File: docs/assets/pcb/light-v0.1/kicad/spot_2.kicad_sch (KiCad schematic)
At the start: 7 parts, among them J10 SPOT 2, J11 SPOT 3, J9 SPOT 1, U500 27V flat-clamp transient prot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

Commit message: Refresh PCB chapters from verified central LED snapshots
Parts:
- C523, C524: Manufacturer (none) -> Murata
- D504: Manufacturer (none) -> Diodes Incorporated
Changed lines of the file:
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@@
         (font
           (size 1.0 1.0))))
-    (property "Manufacturer" ""
+    (property "Manufacturer" "Diodes Incorporated"
       (at 175.26 180.34 0.0)
       (hide yes)
@@
         (font
           (size 1.0 1.0))))
-    (property "Manufacturer" ""
+    (property "Manufacturer" "Murata"
       (at 43.18 180.34 0.0)
       (hide yes)
@@
         (font
           (size 1.0 1.0))))
-    (property "Manufacturer" ""
+    (property "Manufacturer" "Murata"
       (at 96.52 180.34 0.0)
       (hide yes)

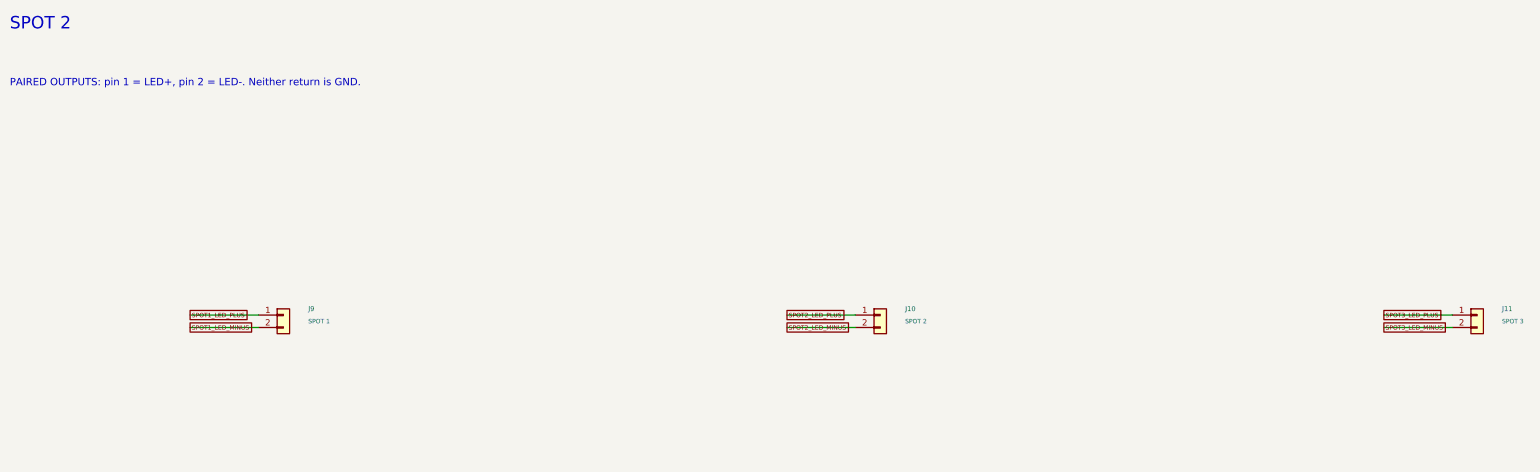
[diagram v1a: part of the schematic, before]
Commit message: Refresh PCB chapters for grouped arm connectors and branded revision
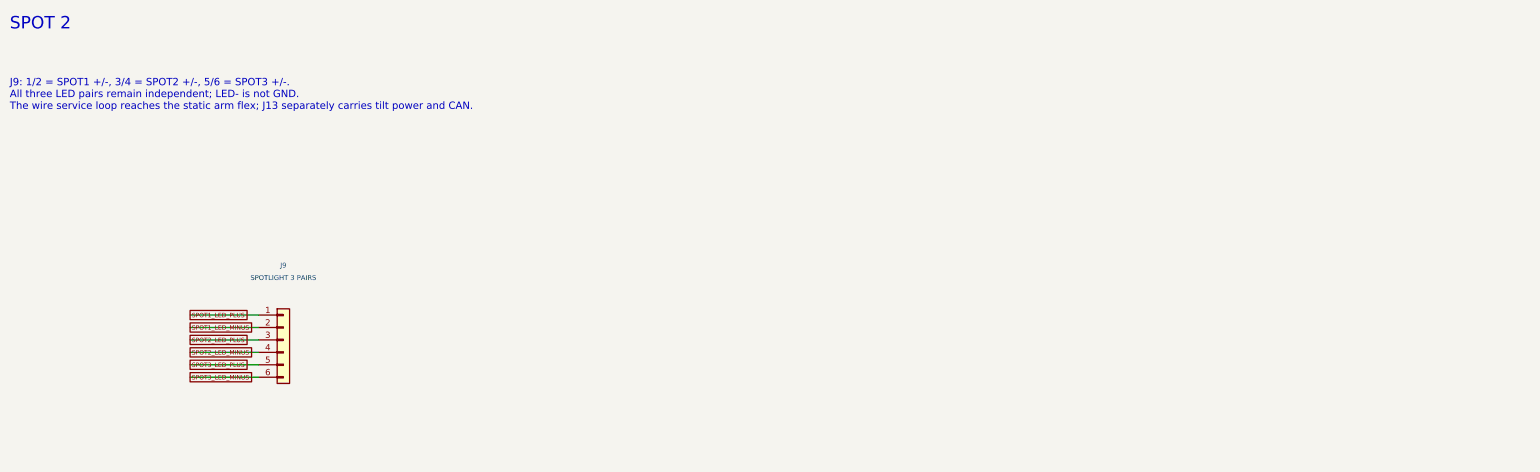
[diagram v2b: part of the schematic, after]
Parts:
- removed J10: SPOT 2, ELF:Enclosure_J10, symbol Connector_Generic:Conn_01x02
- removed J11: SPOT 3, Connector_JST:JST_GH_BM02B-GHS-TBT_1x02-1MP_P1.25mm_Vertical, symbol Connector_Generic:Conn_01x02
- J9: value SPOT 1 -> SPOTLIGHT 3 PAIRS; footprint ELF:Enclosure_J9 -> EL:JST_GH_BM06B-GHS-TBT_1x06-1MP_P1.25mm_Vertical; symbol Connector_Generic:Conn_01x02 -> Connector_Generic:Conn_01x06; MPN BM02B-GHS-TBT(LF)(SN) -> BM06B-GHS-TBT(LF)(SN)
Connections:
- net SPOT2_LED_MINUS: now also J9.4 (Pin_4)
- net SPOT2_LED_PLUS: now also J9.3 (Pin_3)
- net SPOT3_LED_MINUS: now also J9.6 (Pin_6)
- net SPOT3_LED_PLUS: now also J9.5 (Pin_5)
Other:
- note added: "J9: 1/2 = SPOT1 +/-, 3/4 = SPOT2 +/-, 5/6 = SPOT3 +/-. All three LED pairs remain independent; LED- is not GND. The wire service loop reaches the static arm flex; J13 separately carries tilt power and CAN."
- note removed: "PAIRED OUTPUTS: pin 1 = LED+, pin 2 = LED-. Neither return is GND."
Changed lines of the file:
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@@
         (font
           (size 1.0 1.0)))))
+  (wire
+    (pts
+      (xy 43.18 176.53)
+      (xy 96.52 176.53))
+    (stroke
+      (width 0)
+      (type default))
+)
+  (global_label "V24_SPOT"
+    (shape passive)
+    (at 96.52 176.53 0)
+    (effects
+      (font
+        (size 0.9 0.9))
+      (justify left))
+    (property "Intersheetrefs" "${INTERSHEET_REFS}"
+      (at 96.52 176.53 0.0)
+      (hide yes)
+      (effects
+        (font
+          (size 1.0 1.0)))))
+  (text "SPOT 2"
+    (at 20.32 15.24 0)
+    (effects
+      (font
+        (size 2.54 2.54))
+      (justify left top))
+)
+  (text "J9: 1/2 = SPOT1 +/-, 3/4 = SPOT2 +/-, 5/6 = SPOT3 +/-.\nAll three LED pairs remain independent; LED- is not GND.\nThe wire service loop reaches the static arm flex; J13 separately carries tilt power and CAN."
+    (at 20.32 27.94 0)
+    (effects
+      (font
+        (size 1.5 1.5))
+      (justify left top))
+)
+  (text "CH3 current loop continuation from U9 on spot_1"
+    (at 20.32 132.08 0)
+    (effects
+      (font
+        (size 1.8 1.8))
+      (justify left top))
+)
+  (text "U500 local spotlight-rail shunt clamp.\nPulse limits do not establish continuous braking."
+    (at 241.3 228.6 0)
+    (effects
+      (font
+        (size 1.27 1.27))
+      (justify left top))
+)
+  (embedded_fonts no)
   (symbol
-    (lib_id "Connector_Generic:Conn_01x02")
-    (at 76.2 76.2 0)
+    (lib_id "Connector_Generic:Conn_01x06")
+    (at 76.2 81.28 0)
     (unit 1)
     (exclude_from_sim yes)
@@
     (dnp no)
     (property "Reference" "J9"
-      (at 81.28 74.93 0.0)
-      (effects
-        (font
-          (size 1.0 1.0))
-        (justify left)))
-    (property "Value" "SPOT 1"
-      (at 81.28 77.47 0.0)
-      (effects
-        (font
-          (size 0.9 0.9))
-        (justify left)))
-    (property "Footprint" "ELF:Enclosure_J9"
-      (at 76.2 76.2 0.0)
-      (hide yes)
-      (effects
-        (font
-          (size 1.0 1.0))))
-    (property "MPN" "BM02B-GHS-TBT(LF)(SN)"
-      (at 76.2 76.2 0.0)
+      (at 76.2 66.04 0.0)
+      (effects
+        (font
+          (size 1.0 1.0))))
+    (property "Value" "SPOTLIGHT 3 PAIRS"
+      (at 76.2 68.58 0.0)
+      (effects
+        (font
+          (size 1.0 1.0))))
+    (property "Footprint" "EL:JST_GH_BM06B-GHS-TBT_1x06-1MP_P1.25mm_Vertical"
+      (at 76.2 81.28 0.0)
+      (hide yes)
+      (effects
+        (font
+          (size 1.0 1.0))))
+    (property "MPN" "BM06B-GHS-TBT(LF)(SN)"
+      (at 76.2 81.28 0.0)
       (hide yes)
       (effects
@@
           (size 1.0 1.0))))
     (property "Manufacturer" "JST"
-      (at 76.2 76.2 0.0)
+      (at 76.2 81.28 0.0)
       (hide yes)
       (effects
@@
           (size 1.0 1.0))))
     (property "Datasheet" "https://www.jst-mfg.com/product/pdf/eng/eGH.pdf"
-      (at 76.2 76.2 0.0)
+      (at 76.2 81.28 0.0)
       (hide yes)
       (effects
@@
 )
     (pin "2"
+)
+    (pin "3"
+)
+    (pin "4"
+)
+    (pin "5"
+)
+    (pin "6"
 ))
   (wire
@@
         (font
           (size 1.0 1.0)))))
-  (symbol
-    (lib_id "Connector_Generic:Conn_01x02")
-    (at 198.12 76.2 0)
-    (unit 1)
-    (exclude_from_sim yes)
-    (in_bom yes)
-    (on_board yes)
-    (dnp no)
-    (property "Reference" "J10"
-      (at 203.2 74.93 0.0)
-      (effects
-        (font
-          (size 1.0 1.0))
-        (justify left)))
-    (property "Value" "SPOT 2"
-      (at 203.2 77.47 0.0)
-      (effects
-        (font
-          (size 0.9 0.9))
-        (justify left)))
-    (property "Footprint" "ELF:Enclosure_J10"
-      (at 198.12 76.2 0.0)
-      (hide yes)
-      (effects
-        (font
-          (size 1.0 1.0))))
-    (property "MPN" "BM02B-GHS-TBT(LF)(SN)"
-      (at 198.12 76.2 0.0)
-      (hide yes)
-      (effects
-        (font
-          (size 1.0 1.0))))
-    (property "Manufacturer" "JST"
-      (at 198.12 76.2 0.0)
-      (hide yes)
-      (effects
-        (font
-          (size 1.0 1.0))))
-    (property "Datasheet" "https://www.jst-mfg.com/product/pdf/eng/eGH.pdf"
-      (at 198.12 76.2 0.0)
-      (hide yes)
-      (effects
-        (font
-          (size 1.0 1.0))))
-    (instances
-      (project "engineered-lighting-rev-a"
-        (path "/964013ac-cca6-5de7-b648-d598a25a58e0/7d811806-cdea-579b-88fd-298c7067c42f"
-          (reference "J10")
-          (unit 1))))
-    (pin "1"
-)
-    (pin "2"
-))
-  (wire
-    (pts
-      (xy 193.04 76.2)
-      (xy 179.07 76.2))
+  (wire
+    (pts
+      (xy 71.12 81.28)
+      (xy 57.15 81.28))
     (stroke
       (width 0)
@@
   (global_label "SPOT2_LED_PLUS"
     (shape passive)
-    (at 179.07 76.2 0.0)
-    (effects
-      (font
-        (size 0.9 0.9))
-      (justify left))
-    (property "Intersheetrefs" "${INTERSHEET_REFS}"
-      (at 179.07 76.2 0.0)
-      (hide yes)
-      (effects
-        (font
-          (size 1.0 1.0)))))
-  (wire
-    (pts
-      (xy 193.04 78.74)
-      (xy 179.07 78.74))
+    (at 57.15 81.28 0.0)
+    (effects
+      (font
+        (size 0.9 0.9))
+      (justify left))
+    (property "Intersheetrefs" "${INTERSHEET_REFS}"
+      (at 57.15 81.28 0.0)
+      (hide yes)
+      (effects
+        (font
+          (size 1.0 1.0)))))
+  (wire
+    (pts
+      (xy 71.12 83.82)
+      (xy 57.15 83.82))
     (stroke
       (width 0)
@@
   (global_label "SPOT2_LED_MINUS"
     (shape passive)
-    (at 179.07 78.74 0.0)
-    (effects
-      (font
-        (size 0.9 0.9))
-      (justify left))
-    (property "Intersheetrefs" "${INTERSHEET_REFS}"
-      (at 179.07 78.74 0.0)
-      (hide yes)
-      (effects
-        (font
-          (size 1.0 1.0)))))
-  (symbol
-    (lib_id "Connector_Generic:Conn_01x02")
-    (at 320.04 76.2 0)
-    (unit 1)
-    (exclude_from_sim yes)
-    (in_bom yes)
-    (on_board yes)
-    (dnp no)
-    (property "Reference" "J11"
-      (at 325.12 74.93 0.0)
-      (effects
-        (font
-          (size 1.0 1.0))
-        (justify left)))
-    (property "Value" "SPOT 3"
-      (at 325.12 77.47 0.0)
-      (effects
-        (font
-          (size 0.9 0.9))
-        (justify left)))
-    (property "Footprint" "Connector_JST:JST_GH_BM02B-GHS-TBT_1x02-1MP_P1.25mm_Vertical"
-      (at 320.04 76.2 0.0)
-      (hide yes)
-      (effects
-        (font
-          (size 1.0 1.0))))
-    (property "MPN" "BM02B-GHS-TBT(LF)(SN)"
-      (at 320.04 76.2 0.0)
-      (hide yes)
-      (effects
-        (font
-          (size 1.0 1.0))))
-    (property "Manufacturer" "JST"
-      (at 320.04 76.2 0.0)
-      (hide yes)
-      (effects
-        (font
-          (size 1.0 1.0))))
-    (property "Datasheet" "https://www.jst-mfg.com/product/pdf/eng/eGH.pdf"
-      (at 320.04 76.2 0.0)
-      (hide yes)
-      (effects
-        (font
-          (size 1.0 1.0))))
-    (instances
-      (project "engineered-lighting-rev-a"
-        (path "/964013ac-cca6-5de7-b648-d598a25a58e0/7d811806-cdea-579b-88fd-298c7067c42f"
-          (reference "J11")
-          (unit 1))))
-    (pin "1"
-)
-    (pin "2"
-))
-  (wire
-    (pts
-      (xy 314.96 76.2)
-      (xy 300.99 76.2))
+    (at 57.15 83.82 0.0)
+    (effects
+      (font
+        (size 0.9 0.9))
+      (justify left))
+    (property "Intersheetrefs" "${INTERSHEET_REFS}"
+      (at 57.15 83.82 0.0)
+      (hide yes)
+      (effects
+        (font
+          (size 1.0 1.0)))))
+  (wire
+    (pts
+      (xy 71.12 86.36)
+      (xy 57.15 86.36))
     (stroke
       (width 0)
@@
   (global_label "SPOT3_LED_PLUS"
     (shape passive)
-    (at 300.99 76.2 0.0)
-    (effects
-      (font
-        (size 0.9 0.9))
-      (justify left))
-    (property "Intersheetrefs" "${INTERSHEET_REFS}"
-      (at 300.99 76.2 0.0)
-      (hide yes)
-      (effects
-        (font
-          (size 1.0 1.0)))))
-  (wire
-    (pts
-      (xy 314.96 78.74)
-      (xy 300.99 78.74))
+    (at 57.15 86.36 0.0)
+    (effects
+      (font
+        (size 0.9 0.9))
+      (justify left))
+    (property "Intersheetrefs" "${INTERSHEET_REFS}"
+      (at 57.15 86.36 0.0)
+      (hide yes)
+      (effects
+        (font
+          (size 1.0 1.0)))))
+  (wire
+    (pts
+      (xy 71.12 88.9)
+      (xy 57.15 88.9))
     (stroke
       (width 0)
@@
   (global_label "SPOT3_LED_MINUS"
     (shape passive)
-    (at 300.99 78.74 0.0)
-    (effects
-      (font
-        (size 0.9 0.9))
-      (justify left))
-    (property "Intersheetrefs" "${INTERSHEET_REFS}"
-      (at 300.99 78.74 0.0)
-      (hide yes)
-      (effects
-        (font
-          (size 1.0 1.0)))))
-  (wire
-    (pts
-      (xy 43.18 176.53)
-      (xy 96.52 176.53))
-    (stroke
-      (width 0)
-      (type default))
-)
-  (global_label "V24_SPOT"
-    (shape passive)
-    (at 96.52 176.53 0)
-    (effects
-      (font
-        (size 0.9 0.9))
-      (justify left))
-    (property "Intersheetrefs" "${INTERSHEET_REFS}"
-      (at 96.52 176.53 0.0)
-      (hide yes)
-      (effects
-        (font
-          (size 1.0 1.0)))))
-  (text "SPOT 2"
-    (at 20.32 15.24 0)
-    (effects
-      (font
-        (size 2.54 2.54))
-      (justify left top))
-)
-  (text "PAIRED OUTPUTS: pin 1 = LED+, pin 2 = LED-. Neither return is GND."
-    (at 20.32 27.94 0)
-    (effects
-      (font
-        (size 1.5 1.5))
-      (justify left top))
-)
-  (text "CH3 current loop continuation from U9 on spot_1"
-    (at 20.32 132.08 0)
-    (effects
-      (font
-        (size 1.8 1.8))
-      (justify left top))
-)
-  (text "U500 local spotlight-rail shunt clamp.\nPulse limits do not establish continuous braking."
-    (at 241.3 228.6 0)
-    (effects
-      (font
-        (size 1.27 1.27))
-      (justify left top))
-)
-  (embedded_fonts no))
+    (at 57.15 88.9 0.0)
+    (effects
+      (font
+        (size 0.9 0.9))
+      (justify left))
+    (property "Intersheetrefs" "${INTERSHEET_REFS}"
+      (at 57.15 88.9 0.0)
+      (hide yes)
+      (effects
+        (font
+          (size 1.0 1.0))))))
